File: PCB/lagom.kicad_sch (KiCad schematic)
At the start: 167 parts, among them J1 Conn_01x04, J2 Conn_01x03, SW83 RotaryEncoder_Switch, SW84 RotaryEncoder_Switch, U1 ProMicro, U2 74HC138, U3 74HC138

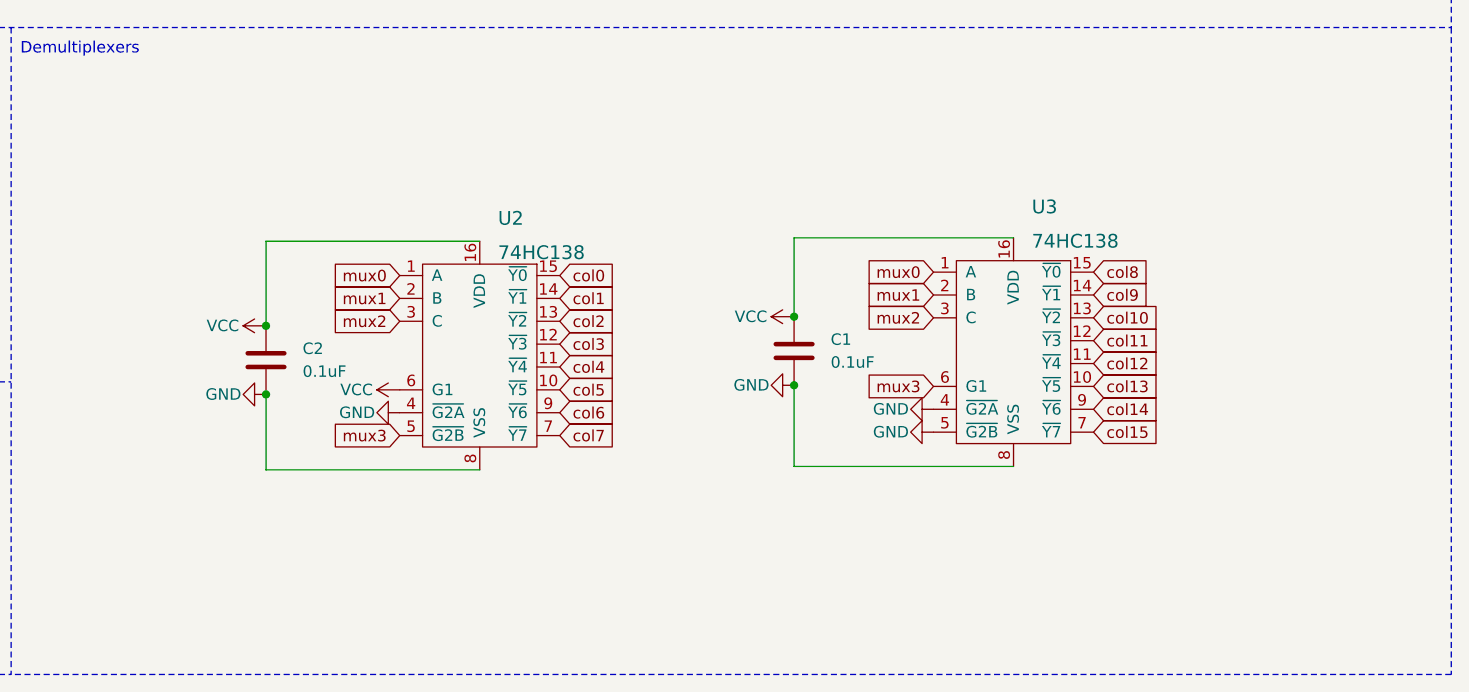
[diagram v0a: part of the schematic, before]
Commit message: Replace 74hc138 symbol with standard library symbol and remove custom library
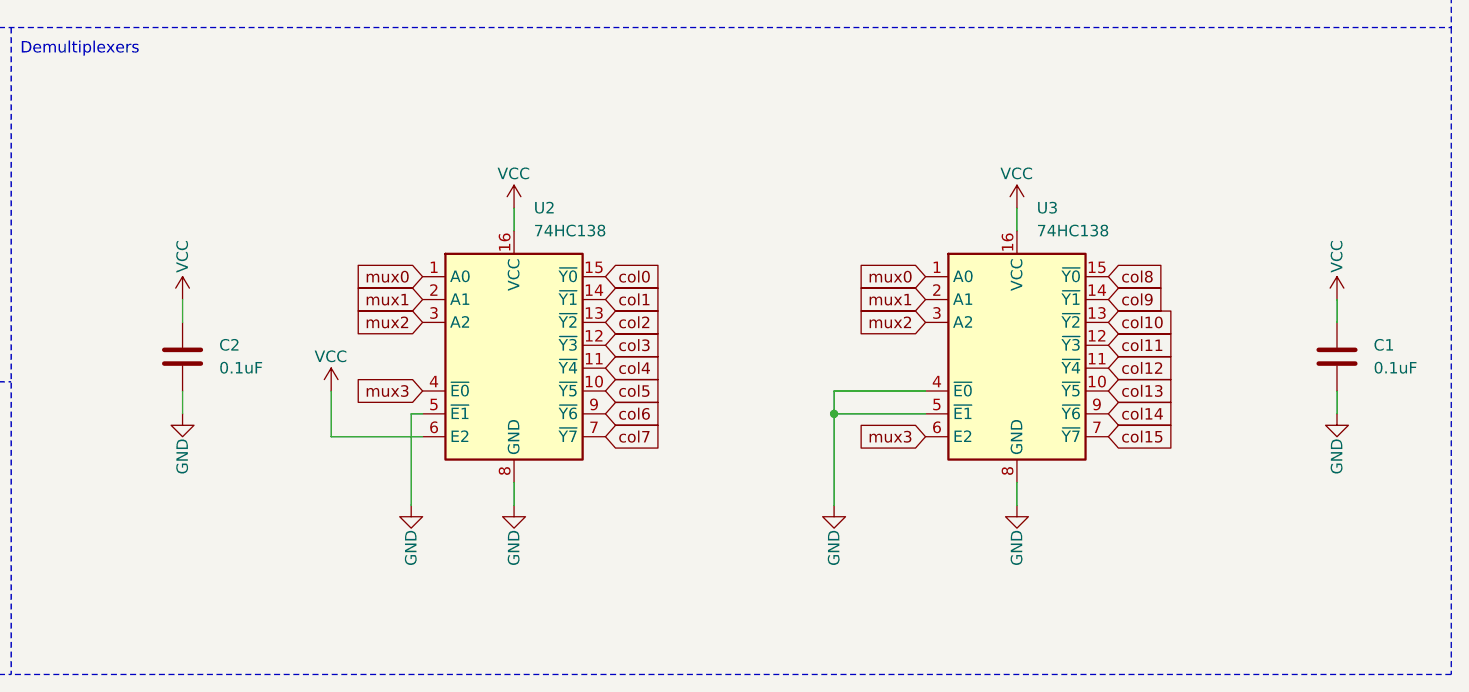
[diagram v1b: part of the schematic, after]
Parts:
- removed U2, U3: 74HC138, Package_DIP:DIP-16_W7.62mm_Socket, symbol w_logic:74HC138
- added U2, U3: 74HC138, symbol 74xx:74HC138
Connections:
- net GND: now also U2.5 (~{E1}), U2.8 (GND), U3.4 (~{E0}), U3.5 (~{E1}), U3.8 (GND)
- net RotB: now also U3.7 (~{Y7})
- net VCC: now also U2.16 (VCC), U2.6 (E2), U3.16 (VCC)
- net col0: now also U2.15 (~{Y0})
- net col1: now also U2.14 (~{Y1})
- net col10: now also U3.13 (~{Y2})
- net col11: now also U3.12 (~{Y3})
- net col12: now also U3.11 (~{Y4})
- net col13: now also U3.10 (~{Y5})
- net col14: now also U3.9 (~{Y6})
- net col2: now also U2.13 (~{Y2})
- net col3: now also U2.12 (~{Y3})
- net col4: now also U2.11 (~{Y4})
- net col5: now also U2.10 (~{Y5})
- net col6: now also U2.9 (~{Y6})
- net col7: now also U2.7 (~{Y7})
- net col8: now also U3.15 (~{Y0})
- net col9: now also U3.14 (~{Y1})
- net mux0: now also U2.1 (A0), U3.1 (A0)
- net mux1: now also U2.2 (A1), U3.2 (A1)
- net mux2: now also U2.3 (A2), U3.3 (A2)
- net mux3: now also U2.4 (~{E0}), U3.6 (E2)
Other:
- moved on the sheet: C1, C2

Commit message: Demultiplexer footprint -> TSSOP16
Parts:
- U2, U3: footprint (none) -> Package_SO:TSSOP-16_4.4x5mm_P0.65mm
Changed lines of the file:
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@@
 			)
 		)
-		(property "Footprint" ""
+		(property "Footprint" "Package_SO:TSSOP-16_4.4x5mm_P0.65mm"
 			(at 347.98 182.88 0)
 			(effects
@@
 			)
 		)
-		(property "Footprint" ""
+		(property "Footprint" "Package_SO:TSSOP-16_4.4x5mm_P0.65mm"
 			(at 292.1 182.88 0)
 			(effects

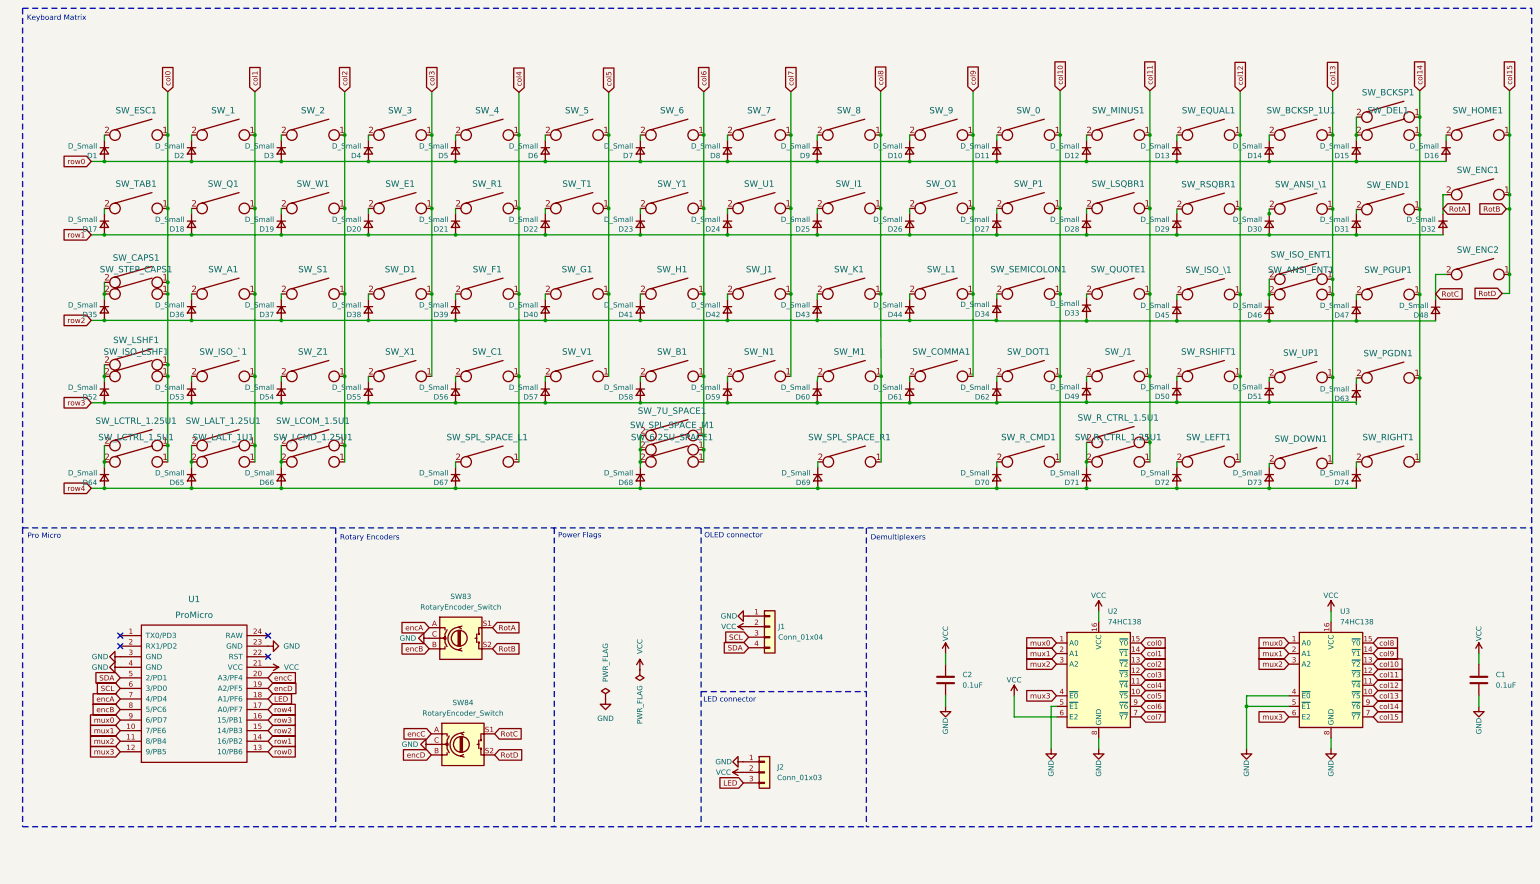
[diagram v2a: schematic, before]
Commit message: Remove optional ANSI from schematic
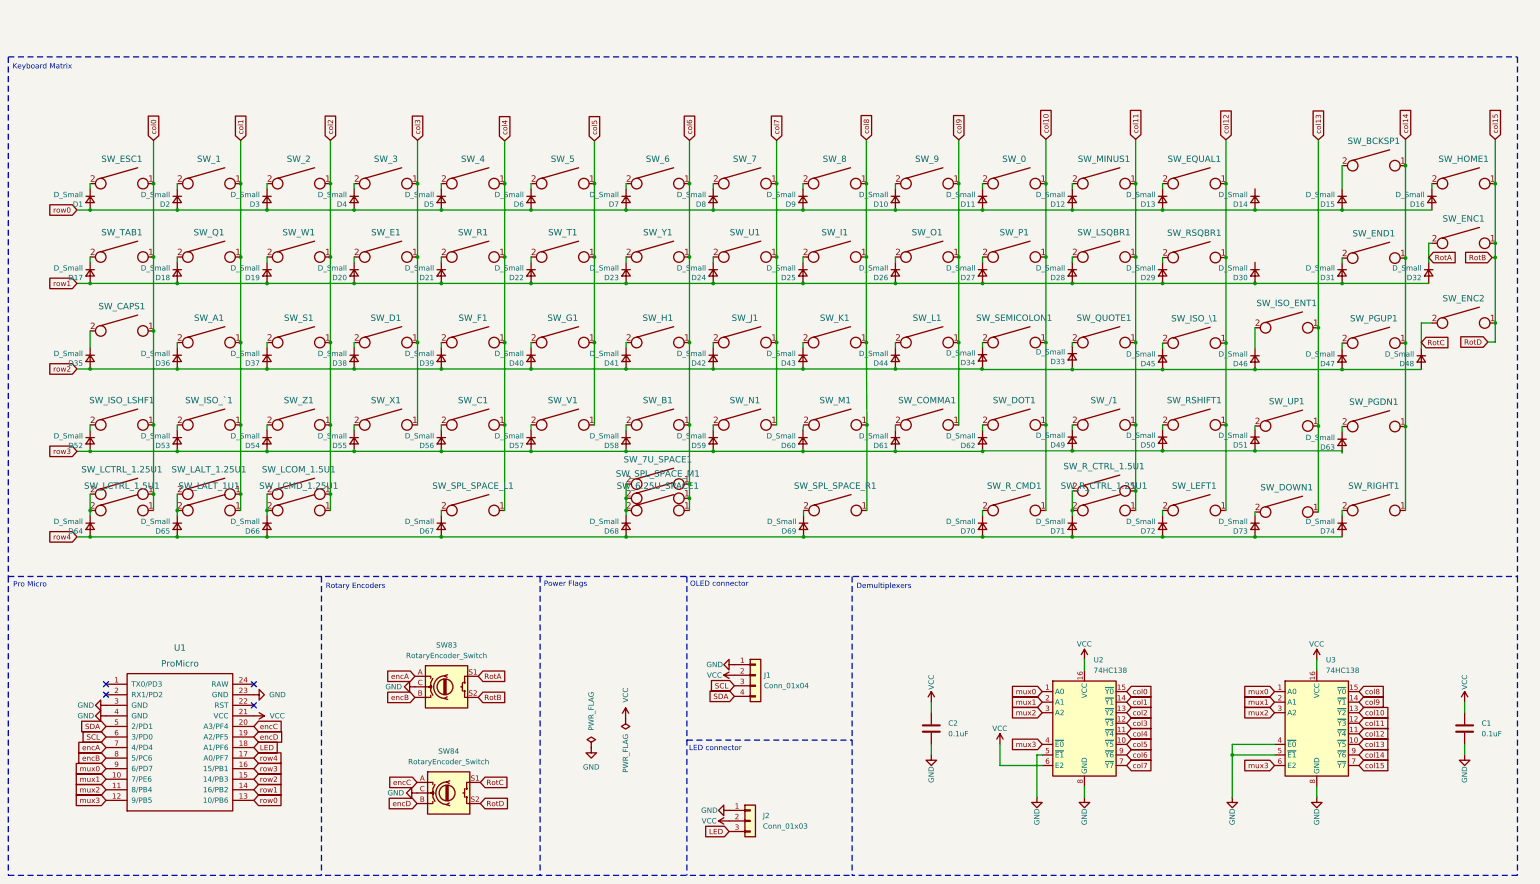
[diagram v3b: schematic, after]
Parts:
- removed SW_ANSI_ENT1, SW_LSHF1: KEYSW, Button_Switch_Keyboard:SW_Cherry_MX_2.25u_PCB, symbol keyboard_parts:KEYSW
- removed SW_ANSI_\1: KEYSW, Button_Switch_Keyboard:SW_Cherry_MX_1.50u_PCB, symbol keyboard_parts:KEYSW
- removed SW_BCKSP_1U1, SW_DEL1: KEYSW, Button_Switch_Keyboard:SW_Cherry_MX_1.00u_PCB, symbol keyboard_parts:KEYSW
- removed SW_STEP_CAPS1: KEYSW, Button_Switch_Keyboard:SW_Cherry_MX_1.25u_PCB, symbol keyboard_parts:KEYSW
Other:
- moved on the sheet: C1, C2, D1, D10, D11, D12, D13, D14, D15, D16, D17, D18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

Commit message: Standard SW_PUSH symbol. Remove unused library and submodule
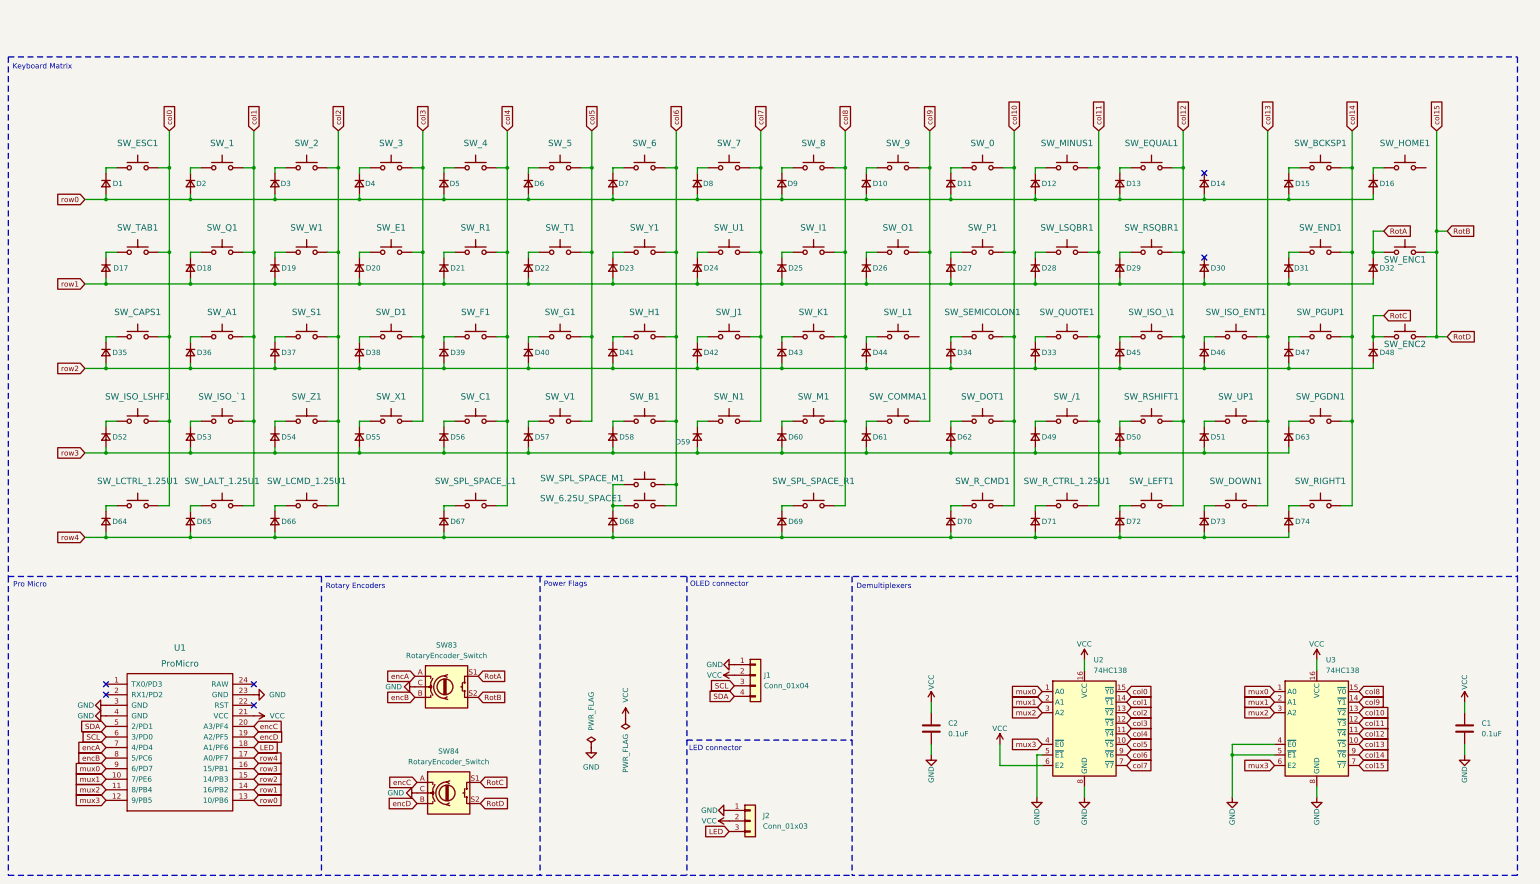
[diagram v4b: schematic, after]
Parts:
- removed SW_7U_SPACE1: KEYSW, Button_Switch_Keyboard:SW_Cherry_MX_7u_PCB, symbol keyboard_parts:KEYSW
- removed SW_LALT_1U1: KEYSW, Button_Switch_Keyboard:SW_Cherry_MX_1.00u_PCB, symbol keyboard_parts:KEYSW
- removed SW_LCOM_1.5U1, SW_LCTRL_1.5U1, SW_R_CTRL_1.5U1: KEYSW, Button_Switch_Keyboard:SW_Cherry_MX_1.50u_PCB, symbol keyboard_parts:KEYSW
- SW_/1, SW_0, SW_1, SW_2, SW_3, SW_4, SW_5, SW_6, SW_6.25U_SPACE1, SW_7, SW_8, SW_9, SW_A1, SW_B1, SW_BCKSP1, SW_C1, SW_CAPS1, SW_COMMA1, SW_D1, SW_DOT1, SW_DOWN1, SW_E1, SW_ENC1, SW_ENC2, SW_END1, SW_EQUAL1, SW_ESC1, SW_F1, SW_G1, SW_H1, SW_HOME1, SW_I1, SW_ISO_ENT1, SW_ISO_LSHF1, SW_ISO_\1, SW_ISO_`1, SW_J1, SW_K1, SW_L1, SW_LALT_1.25U1, SW_LCMD_1.25U1, SW_LCTRL_1.25U1, SW_LEFT1, SW_LSQBR1, SW_M1, SW_MINUS1, SW_N1, SW_O1, SW_P1, SW_PGDN1, SW_PGUP1, SW_Q1, SW_QUOTE1, SW_R1, SW_RIGHT1, SW_RSHIFT1, SW_RSQBR1, SW_R_CMD1, SW_R_CTRL_1.25U1, SW_S1, SW_SEMICOLON1, SW_SPL_SPACE_L1, SW_SPL_SPACE_M1, SW_SPL_SPACE_R1, SW_T1, SW_TAB1, SW_U1, SW_UP1, SW_V1, SW_W1, SW_X1, SW_Y1, SW_Z1: symbol keyboard_parts:KEYSW -> Switch:SW_Push
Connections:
- net RotA: now also SW_ENC1.1; no longer SW_ENC1.2
- net RotB: now also SW_ENC1.2, SW_ENC2.2; no longer SW_ENC1.1, SW_ENC2.1, SW_HOME1.1
- net RotC: now also SW_ENC2.1; no longer SW_ENC2.2
- net col0: now also SW_CAPS1.2, SW_ESC1.2, SW_ISO_LSHF1.2, SW_LCTRL_1.25U1.2, SW_TAB1.2; no longer SW_CAPS1.1, SW_ESC1.1, SW_ISO_LSHF1.1, SW_LCTRL_1.25U1.1, SW_TAB1.1
- net col1: now also SW_1.2, SW_A1.2, SW_ISO_`1.2, SW_LALT_1.25U1.2, SW_Q1.2; no longer SW_1.1, SW_A1.1, SW_ISO_`1.1, SW_LALT_1.25U1.1, SW_Q1.1
- net col10: now also SW_0.2, SW_DOT1.2, SW_P1.2, SW_R_CMD1.2, SW_SEMICOLON1.2; no longer SW_0.1, SW_DOT1.1, SW_P1.1, SW_R_CMD1.1, SW_SEMICOLON1.1
- net col11: now also SW_/1.2, SW_LSQBR1.2, SW_MINUS1.2, SW_QUOTE1.2, SW_R_CTRL_1.25U1.2; no longer SW_/1.1, SW_LSQBR1.1, SW_MINUS1.1, SW_QUOTE1.1, SW_R_CTRL_1.25U1.1
- net col12: now also SW_EQUAL1.2, SW_ISO_\1.2, SW_LEFT1.2, SW_RSHIFT1.2, SW_RSQBR1.2; no longer SW_EQUAL1.1, SW_ISO_\1.1, SW_LEFT1.1, SW_RSHIFT1.1, SW_RSQBR1.1
- net col13: now also SW_DOWN1.2, SW_ISO_ENT1.2, SW_UP1.2; no longer SW_DOWN1.1, SW_ISO_ENT1.1, SW_UP1.1
- net col14: now also SW_BCKSP1.2, SW_END1.2, SW_PGDN1.2, SW_PGUP1.2, SW_RIGHT1.2; no longer SW_BCKSP1.1, SW_END1.1, SW_PGDN1.1, SW_PGUP1.1, SW_RIGHT1.1
- net col2: now also SW_2.2, SW_LCMD_1.25U1.2, SW_S1.2, SW_W1.2, SW_Z1.2; no longer SW_2.1, SW_LCMD_1.25U1.1, SW_S1.1, SW_W1.1, SW_Z1.1
- net col3: now also SW_3.2, SW_D1.2, SW_E1.2, SW_X1.2; no longer SW_3.1, SW_D1.1, SW_E1.1, SW_X1.1
- net col4: now also SW_4.2, SW_C1.2, SW_F1.2, SW_R1.2, SW_SPL_SPACE_L1.2; no longer SW_4.1, SW_C1.1, SW_F1.1, SW_R1.1, SW_SPL_SPACE_L1.1
- net col5: now also SW_5.2, SW_G1.2, SW_T1.2, SW_V1.2; no longer SW_5.1, SW_G1.1, SW_T1.1, SW_V1.1
- net col6: now also SW_6.2, SW_6.25U_SPACE1.2, SW_B1.2, SW_H1.2, SW_SPL_SPACE_M1.2, SW_Y1.2; no longer SW_6.1, SW_6.25U_SPACE1.1, SW_B1.1, SW_H1.1, SW_SPL_SPACE_M1.1, SW_Y1.1
- net col7: now also SW_7.2, SW_J1.2, SW_N1.2, SW_U1.2; no longer SW_7.1, SW_J1.1, SW_N1.1, SW_U1.1
- net col8: now also SW_8.2, SW_I1.2, SW_K1.2, SW_M1.2, SW_SPL_SPACE_R1.2; no longer SW_8.1, SW_I1.1, SW_K1.1, SW_M1.1, SW_SPL_SPACE_R1.1
- net col9: now also SW_9.2, SW_COMMA1.2, SW_O1.2; no longer SW_9.1, SW_COMMA1.1, SW_L1.1, SW_O1.1
- net at D43.1 (K): now also SW_K1.1; no longer SW_K1.2
- net at D34.1 (K): now also SW_SEMICOLON1.1; no longer SW_SEMICOLON1.2
- net at D4.1 (K): now also SW_3.1; no longer SW_3.2
- net at D50.1 (K): now also SW_RSHIFT1.1; no longer SW_RSHIFT1.2
- net at D54.1 (K): now also SW_Z1.1; no longer SW_Z1.2
- net at D1.1 (K): now also SW_ESC1.1; no longer SW_ESC1.2
- net at D11.1 (K): now also SW_0.1; no longer SW_0.2
- net at D23.1 (K): now also SW_Y1.1; no longer SW_Y1.2
- net at D17.1 (K): now also SW_TAB1.1; no longer SW_TAB1.2
- net at D38.1 (K): now also SW_D1.1; no longer SW_D1.2
- net at D36.1 (K): now also SW_A1.1; no longer SW_A1.2
- net at D44.1 (K): now also SW_L1.1; no longer SW_L1.2
- net at D13.1 (K): now also SW_EQUAL1.1; no longer SW_EQUAL1.2
- net at D52.1 (K): now also SW_ISO_LSHF1.1; no longer SW_ISO_LSHF1.2
- net at D27.1 (K): now also SW_P1.1; no longer SW_P1.2
- net at D60.1 (K): now also SW_M1.1; no longer SW_M1.2
- net at D35.1 (K): now also SW_CAPS1.1; no longer SW_CAPS1.2
- net at D25.1 (K): now also SW_I1.1; no longer SW_I1.2
- net at D57.1 (K): now also SW_V1.1; no longer SW_V1.2
- net at D2.1 (K): now also SW_1.1; no longer SW_1.2
- net at D12.1 (K): now also SW_MINUS1.1; no longer SW_MINUS1.2
- net at D61.1 (K): now also SW_COMMA1.1; no longer SW_COMMA1.2
- net at D47.1 (K): now also SW_PGUP1.1; no longer SW_PGUP1.2
- net at D19.1 (K): now also SW_W1.1; no longer SW_W1.2
- net at D56.1 (K): now also SW_C1.1; no longer SW_C1.2
- net at D9.1 (K): now also SW_8.1; no longer SW_8.2
- net at D62.1 (K): now also SW_DOT1.1; no longer SW_DOT1.2
- net at D16.1 (K): now also SW_HOME1.1; no longer SW_HOME1.2
- net at D42.1 (K): now also SW_J1.1; no longer SW_J1.2
- net at D58.1 (K): now also SW_B1.1; no longer SW_B1.2
- net at D26.1 (K): now also SW_O1.1; no longer SW_O1.2
- net at D10.1 (K): now also SW_9.1; no longer SW_9.2
- net at D63.1 (K): now also SW_PGDN1.1; no longer SW_PGDN1.2
- net at D7.1 (K): now also SW_6.1; no longer SW_6.2
- net at D74.1 (K): now also SW_RIGHT1.1; no longer SW_RIGHT1.2
- net at D59.1 (K): now also SW_N1.1; no longer SW_N1.2
- net at D65.1 (K): now also SW_LALT_1.25U1.1; no longer SW_LALT_1.25U1.2
- net at D71.1 (K): now also SW_R_CTRL_1.25U1.1; no longer SW_R_CTRL_1.25U1.2
- net at D22.1 (K): now also SW_T1.1; no longer SW_T1.2
- net at D39.1 (K): now also SW_F1.1; no longer SW_F1.2
- net at D21.1 (K): now also SW_R1.1; no longer SW_R1.2
- net at D66.1 (K): now also SW_LCMD_1.25U1.1; no longer SW_LCMD_1.25U1.2
- net at D67.1 (K): now also SW_SPL_SPACE_L1.1; no longer SW_SPL_SPACE_L1.2
- net at D64.1 (K): now also SW_LCTRL_1.25U1.1; no longer SW_LCTRL_1.25U1.2
- net at D69.1 (K): now also SW_SPL_SPACE_R1.1; no longer SW_SPL_SPACE_R1.2
- net at D31.1 (K): now also SW_END1.1; no longer SW_END1.2
- net at D55.1 (K): now also SW_X1.1; no longer SW_X1.2
- net at D51.1 (K): now also SW_UP1.1; no longer SW_UP1.2
- net at D18.1 (K): now also SW_Q1.1; no longer SW_Q1.2
- net at D8.1 (K): now also SW_7.1; no longer SW_7.2
- net at D29.1 (K): now also SW_RSQBR1.1; no longer SW_RSQBR1.2
- net at D45.1 (K): now also SW_ISO_\1.1; no longer SW_ISO_\1.2
- net at D41.1 (K): now also SW_H1.1; no longer SW_H1.2
- net at D37.1 (K): now also SW_S1.1; no longer SW_S1.2
- net at D5.1 (K): now also SW_4.1; no longer SW_4.2
- net at D6.1 (K): now also SW_5.1; no longer SW_5.2
- net at D40.1 (K): now also SW_G1.1; no longer SW_G1.2
- net at D15.1 (K): now also SW_BCKSP1.1; no longer SW_BCKSP1.2
- net at D72.1 (K): now also SW_LEFT1.1; no longer SW_LEFT1.2
- net at D3.1 (K): now also SW_2.1; no longer SW_2.2
- net at D49.1 (K): now also SW_/1.1; no longer SW_/1.2
- net at D73.1 (K): now also SW_DOWN1.1; no longer SW_DOWN1.2
- net at D20.1 (K): now also SW_E1.1; no longer SW_E1.2
- net at D28.1 (K): now also SW_LSQBR1.1; no longer SW_LSQBR1.2
- net at D53.1 (K): now also SW_ISO_`1.1; no longer SW_ISO_`1.2
- net at D24.1 (K): now also SW_U1.1; no longer SW_U1.2
- net at D70.1 (K): now also SW_R_CMD1.1; no longer SW_R_CMD1.2
- net at D33.1 (K): now also SW_QUOTE1.1; no longer SW_QUOTE1.2
- net at D46.1 (K): now also SW_ISO_ENT1.1; no longer SW_ISO_ENT1.2
- new net: D68.1 (K), SW_6.25U_SPACE1.1, SW_SPL_SPACE_M1.1
- no-connect marks 4 -> 6
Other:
- moved on the sheet: D1, D10, D11, D12, D13, D14, D15, D16, D17, D18, D19, D2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
